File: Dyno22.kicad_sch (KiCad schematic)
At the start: 50 parts, among them J1 Pwr Input, J2 Display, J3 Pwr Output, J4 BPM & Sensors, J7 UART, SW1 SW_DPST_x2, U1 TS2937CW50, U2 LM324, U3 Demux

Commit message: Amplifier footprint changes
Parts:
- U2: footprint SOIC:SOIC-14_W3.9mm -> Package_DIP:DIP-14_W7.62mm
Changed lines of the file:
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@@
       (effects (font (size 1.27 1.27)) (justify left))
     )
-    (property "Footprint" "SOIC:SOIC-14_W3.9mm" (at 240.03 149.86 0)
+    (property "Footprint" "Package_DIP:DIP-14_W7.62mm" (at 240.03 149.86 0)
       (effects (font (size 1.27 1.27)) hide)
     )
-    (property "Datasheet" "http://www.ti.com/lit/ds/symlink/lm321.pdf" (at 241.3 152.4 0)
+    (property "Datasheet" "https://www.ti.com/lit/ds/symlink/lm224.pdf?HQS=dis-dk-null-digikeymode-dsf-pf-null-wwe&ts=1705778607350" (at 241.3 152.4 0)
       (effects (font (size 1.27 1.27)) hide)
     )

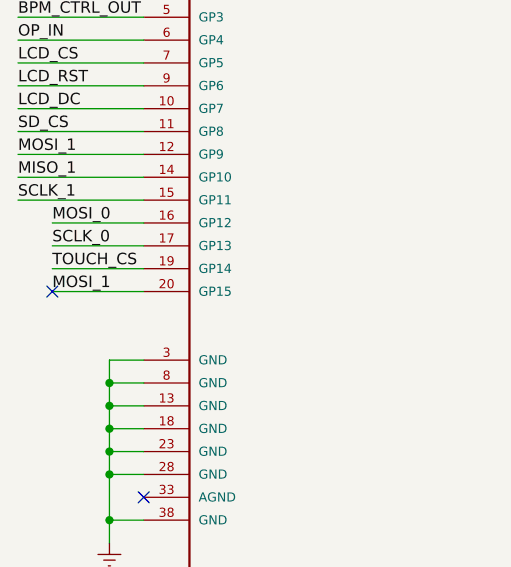
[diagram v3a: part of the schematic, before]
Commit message: Forgot to save schematic changes
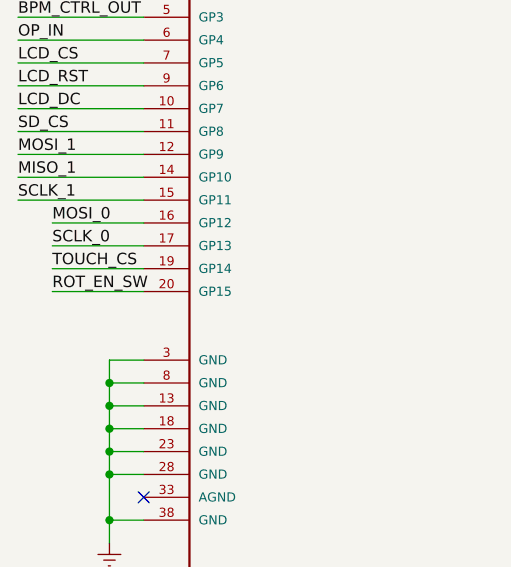
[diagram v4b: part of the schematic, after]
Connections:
- net MOSI_1: no longer A1.20 (GP15)
- net ROT_EN_SW: now also A1.20 (GP15)
- no-connect marks 16 -> 15
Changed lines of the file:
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@@
   (no_connect (at 127 50.8))
   (no_connect (at 63.5 132.08))
-  (no_connect (at 20.32 83.82))
   (no_connect (at 86.36 99.06))
   (no_connect (at 154.94 193.04))
@@
     (effects (font (size 1.27 1.27)) (justify left bottom))
   )
-  (label "MOSI_1" (at 20.32 83.82 0) (fields_autoplaced)
+  (label "ROT_EN_SW" (at 20.32 83.82 0) (fields_autoplaced)
     (effects (font (size 1.27 1.27)) (justify left bottom))
   )
@@
       (effects (font (size 1.27 1.27) italic) hide)
     )
-    (property "Datasheet" "http://www.ti.com/lit/ds/symlink/lm2937.pdf" (at 160.02 40.64 0)
-      (effects (font (size 1.27 1.27)) hide)
-    )
+    (property "Datasheet" "https://services.ts.com.tw/storage/resources/datasheet/TS2937_E15.pdf" (at 160.02 40.64 0)
+      (effects (font (size 1.27 1.27)) hide)
+    )

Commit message: Fix the earth, the earth is our home
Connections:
- net +24V: no longer TP1.1
- net 20V_IN: now reaches F1.1, J1.2 (Pin_2)
- net 20V_IN: now also TP1.1
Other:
- moved on the sheet: TP1

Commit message: Through hole adjustments and some routing changes
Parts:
- TP2, TP3: footprint TestPoint:TestPoint_Loop_D2.60mm_Drill1.6mm_Beaded -> TestPoint:TestPoint_Plated_Hole_D2.0mm
- TP4, TP5: footprint TestPoint:TestPoint_Loop_D2.60mm_Drill1.4mm_Beaded -> TestPoint:TestPoint_Plated_Hole_D2.0mm
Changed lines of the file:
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@@
       (effects (font (size 1.27 1.27)) (justify left))
     )
-    (property "Footprint" "TestPoint:TestPoint_Loop_D2.60mm_Drill1.6mm_Beaded" (at 176.53 22.86 0)
+    (property "Footprint" "TestPoint:TestPoint_Plated_Hole_D2.0mm" (at 176.53 22.86 0)
       (effects (font (size 1.27 1.27)) hide)
     )
@@
       (effects (font (size 1.27 1.27)) (justify left))
     )
-    (property "Footprint" "TestPoint:TestPoint_Loop_D2.60mm_Drill1.4mm_Beaded" (at 130.81 172.72 0)
+    (property "Footprint" "TestPoint:TestPoint_Plated_Hole_D2.0mm" (at 130.81 172.72 0)
       (effects (font (size 1.27 1.27)) hide)
     )
@@
       (effects (font (size 1.27 1.27)) (justify left))
     )
-    (property "Footprint" "TestPoint:TestPoint_Loop_D2.60mm_Drill1.6mm_Beaded" (at 92.71 48.26 0)
+    (property "Footprint" "TestPoint:TestPoint_Plated_Hole_D2.0mm" (at 92.71 48.26 0)
       (effects (font (size 1.27 1.27)) hide)
     )
@@
       (effects (font (size 1.27 1.27)) (justify left))
     )
-    (property "Footprint" "TestPoint:TestPoint_Loop_D2.60mm_Drill1.4mm_Beaded" (at 138.43 63.5 0)
-      (effects (font (size 1.27 1.27)) hide)
-    )
+    (property "Footprint" "TestPoint:TestPoint_Plated_Hole_D2.0mm" (at 138.43 63.5 0)
+      (effects (font (size 1.27 1.27)) hide)
+    )

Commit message: updated encoder
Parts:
- C2: footprint Capacitor_Tantalum_SMD:CP_EIA-6032-20_AVX-F -> CAP_293D-C_VSS:CAP_293D-C_VSS
- Encoder1: footprint Rotary_Encoder:RotaryEncoder_Alps_EC12E-Switch_Vertical_H20mm_CircularMountingHoles -> PEC11R_4215F_S0024:TO_215F-S0024; symbol Device:RotaryEncoder_Switch -> Rotary_Encoder_Kevin:PEC11R-4215F-S0024
- TP1: footprint TestPoint:TestPoint_Loop_D2.60mm_Drill1.4mm_Beaded -> TestPoint:TestPoint_Plated_Hole_D2.0mm
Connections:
- net Earth: now also Encoder1.1, Encoder1.B; no longer Encoder1.C, Encoder1.S2
- net ROT_EN_B: now also Encoder1.C; no longer Encoder1.B
- net ROT_EN_SW: now also Encoder1.2; no longer Encoder1.S1
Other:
- moved on the sheet: TP5
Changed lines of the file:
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@@
   (junction (at 228.6 133.35) (diameter 0) (color 0 0 0 0)
   )
-  (junction (at 130.81 167.64) (diameter 0) (color 0 0 0 0)
-  )
   (junction (at 26.67 93.98) (diameter 0) (color 0 0 0 0)
   )
@@
   (junction (at 127 104.14) (diameter 0) (color 0 0 0 0)
   )
-  (junction (at 130.81 144.78) (diameter 0) (color 0 0 0 0)
-  )
   (junction (at 225.425 108.585) (diameter 0) (color 0 0 0 0)
   )
   (junction (at 85.09 114.3) (diameter 0) (color 0 0 0 0)
   )
+  (junction (at 156.21 143.51) (diameter 0) (color 0 0 0 0)
+  )
   (junction (at 26.67 101.6) (diameter 0) (color 0 0 0 0)
   )
@@
   (junction (at 220.98 52.07) (diameter 0) (color 0 0 0 0)
   )
+  (junction (at 156.21 167.64) (diameter 0) (color 0 0 0 0)
+  )
   (junction (at 26.67 109.22) (diameter 0) (color 0 0 0 0)
   )
@@
     (stroke (width 0) (type default))
   )
+  (wire (pts (xy 156.21 143.51) (xy 156.21 153.67))
+    (stroke (width 0) (type default))
+  )
   (wire (pts (xy 264.16 67.31) (xy 273.685 67.31))
     (stroke (width 0) (type default))
@@
     (stroke (width 0) (type default))
   )
+  (wire (pts (xy 156.21 167.64) (xy 156.21 156.21))
+    (stroke (width 0) (type default))
+  )
   (wire (pts (xy 20.32 78.74) (xy 30.48 78.74))
     (stroke (width 0) (type default))
@@
     (stroke (width 0) (type default))
   )
-  (wire (pts (xy 130.81 151.13) (xy 130.81 144.78))
-    (stroke (width 0) (type default))
-  )
   (wire (pts (xy 260.985 116.205) (xy 272.415 116.205))
     (stroke (width 0) (type default))
@@
     (stroke (width 0) (type default))
   )
-  (wire (pts (xy 114.3 167.64) (xy 130.81 167.64))
+  (wire (pts (xy 114.3 167.64) (xy 156.21 167.64))
     (stroke (width 0) (type default))
   )
@@
     (stroke (width 0) (type default))
   )
-  (wire (pts (xy 120.65 144.78) (xy 130.81 144.78))
-    (stroke (width 0) (type default))
-  )
   (wire (pts (xy 264.16 72.39) (xy 273.685 72.39))
     (stroke (width 0) (type default))
@@
     (stroke (width 0) (type default))
   )
+  (wire (pts (xy 156.21 143.51) (xy 160.02 143.51))
+    (stroke (width 0) (type default))
+  )
   (wire (pts (xy 133.35 63.5) (xy 133.35 64.77))
     (stroke (width 0) (type default))
@@
     (stroke (width 0) (type default))
   )
-  (wire (pts (xy 130.81 167.64) (xy 130.81 156.21))
-    (stroke (width 0) (type default))
-  )
   (wire (pts (xy 85.09 114.3) (xy 85.09 116.84))
     (stroke (width 0) (type default))
@@
     (stroke (width 0) (type default))
   )
-  (wire (pts (xy 137.16 144.78) (xy 130.81 144.78))
+  (wire (pts (xy 120.65 143.51) (xy 156.21 143.51))
     (stroke (width 0) (type default))
   )
@@
     (stroke (width 0) (type default))
   )
-  (wire (pts (xy 120.65 143.51) (xy 120.65 144.78))
-    (stroke (width 0) (type default))
-  )
   (wire (pts (xy 181.61 152.4) (xy 190.5 152.4))
     (stroke (width 0) (type default))
@@
     (effects (font (size 1.27 1.27)) (justify left bottom))
   )
-  (label "ROT_EN_SW" (at 137.16 144.78 0) (fields_autoplaced)
+  (label "ROT_EN_SW" (at 160.02 143.51 0) (fields_autoplaced)
     (effects (font (size 1.27 1.27)) (justify left bottom))
   )
@@
       (effects (font (size 1.27 1.27)) (justify left))
     )
-    (property "Footprint" "Capacitor_Tantalum_SMD:CP_EIA-6032-20_AVX-F" (at 143.51 43.18 0)
+    (property "Footprint" "CAP_293D-C_VSS:CAP_293D-C_VSS" (at 143.51 43.18 0)
       (effects (font (size 1.27 1.27)) hide)
     )
-    (property "Datasheet" "~" (at 143.51 43.18 0)
+    (property "Datasheet" "https://www.vishay.com/docs/40002/293d.pdf" (at 143.51 43.18 0)
       (effects (font (size 1.27 1.27)) hide)
     )
@@
     )
   )
-  (symbol (lib_id "Connector:TestPoint") (at 130.81 167.64 270) (unit 1)
+  (symbol (lib_id "Connector:TestPoint") (at 156.21 167.64 270) (unit 1)
     (in_bom yes) (on_board yes) (dnp no) (fields_autoplaced)
-    (property "Reference" "TP5" (at 135.89 166.37 90)
+    (property "Reference" "TP5" (at 161.29 166.37 90)
       (effects (font (size 1.27 1.27)) (justify left))
     )
-    (property "Value" "GND_TestPoint" (at 135.89 168.91 90)
+    (property "Value" "GND_TestPoint" (at 161.29 168.91 90)
       (effects (font (size 1.27 1.27)) (justify left))
     )
-    (property "Footprint" "TestPoint:TestPoint_Plated_Hole_D2.0mm" (at 130.81 172.72 0)
+    (property "Footprint" "TestPoint:TestPoint_Plated_Hole_D2.0mm" (at 156.21 172.72 0)
       (effects (font (size 1.27 1.27)) hide)
     )
-    (property "Datasheet" "~" (at 130.81 172.72 0)
+    (property "Datasheet" "~" (at 156.21 172.72 0)
       (effects (font (size 1.27 1.27)) hide)
     )
@@
       (effects (font (size 1.27 1.27)))
     )
-    (property "Footprint" "TestPoint:TestPoint_Loop_D2.60mm_Drill1.4mm_Beaded" (at 109.22 45.72 0)
+    (property "Footprint" "TestPoint:TestPoint_Plated_Hole_D2.0mm" (at 109.22 45.72 0)
       (effects (font (size 1.27 1.27)) hide)
     )
@@
     )
   )
-  (symbol (lib_id "Device:RotaryEncoder_Switch") (at 123.19 153.67 0) (unit 1)
+  (symbol (lib_id "Rotary_Encoder_Kevin:PEC11R-4215F-S0024") (at 156.21 156.21 180) (unit 1)
     (in_bom yes) (on_board yes) (dnp no)
-    (property "Reference" "Encoder1" (at 107.95 173.99 0)
+    (property "Reference" "Encoder1" (at 138.43 142.24 0)
       (effects (font (size 1.27 1.27)))
     )
-    (property "Value" "RotaryEncoder_Switch" (at 107.95 176.53 0)
+    (property "Value" "RotaryEncoder_Switch" (at 139.7 139.7 0)
       (effects (font (size 1.27 1.27)))
     )
-    (property "Footprint" "Rotary_Encoder:RotaryEncoder_Alps_EC12E-Switch_Vertical_H20mm_CircularMountingHoles" (at 119.38 149.606 0)
-      (effects (font (size 1.27 1.27)) hide)
+    (property "Footprint" "PEC11R_4215F_S0024:TO_215F-S0024" (at 156.21 156.21 0)
+      (effects (font (size 1.27 1.27) italic) hide)
     )
-    (property "Datasheet" "~" (at 123.19 147.066 0)
-      (effects (font (size 1.27 1.27)) hide)
+    (property "Datasheet" "PEC11R-4215F-S0024" (at 156.21 156.21 0)
+      (effects (font (size 1.27 1.27) italic) hide)
     )
+    (pin "1")
+    (pin "2")
     (pin "A")
     (pin "B")
     (pin "C")
-    (pin "S1")
-    (pin "S2")
     (instances
       (project "Dyno22"

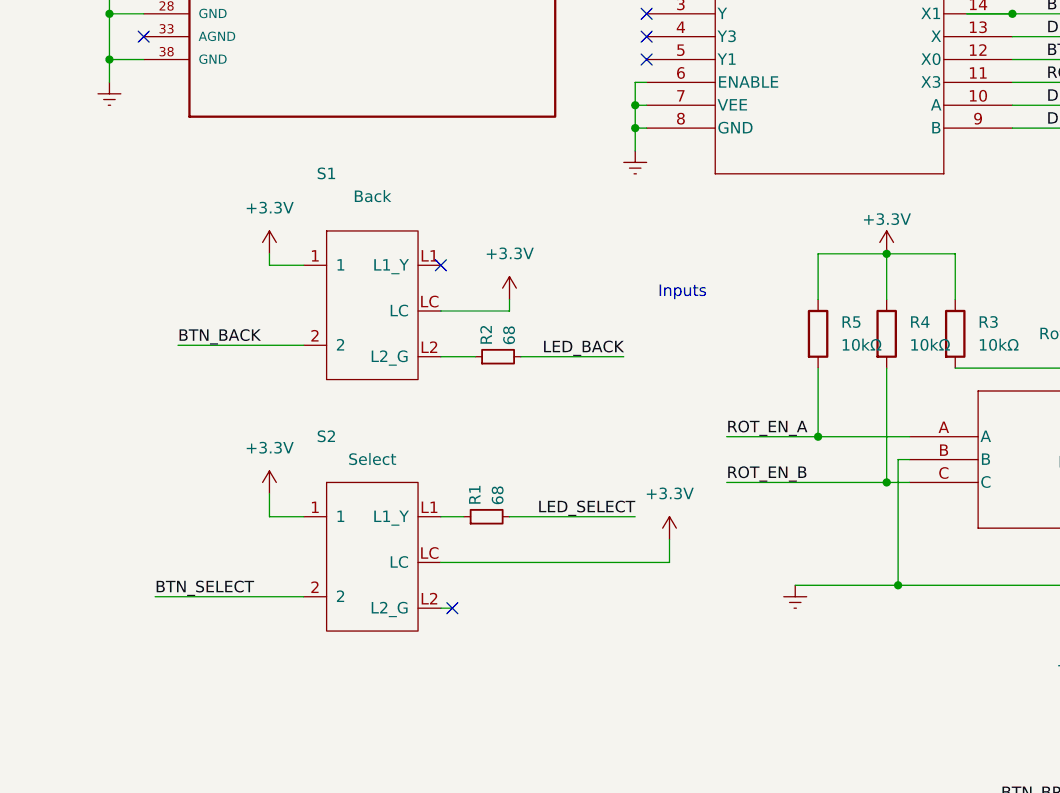
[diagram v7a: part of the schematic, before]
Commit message: added encoder filter circuit
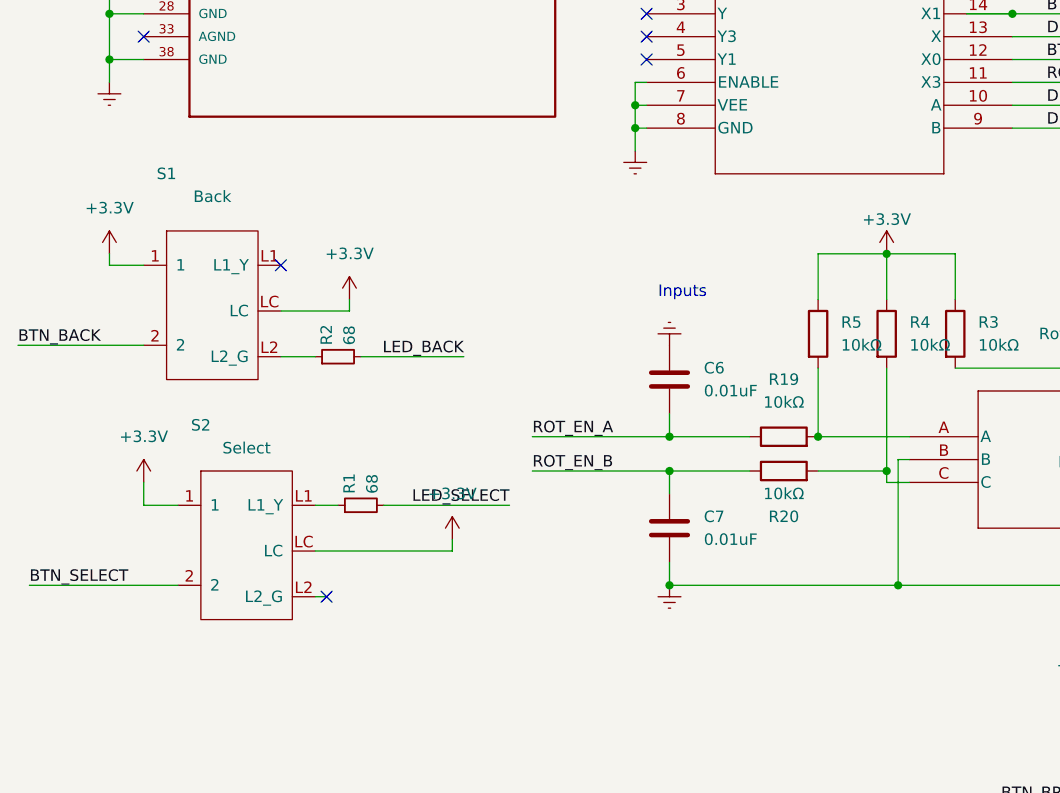
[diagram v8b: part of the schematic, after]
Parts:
- added C6, C7: 0.01uF, Capacitor_SMD:C_0603_1608Metric, symbol Device:C
- added R19, R20: 10kΩ, Resistor_SMD:R_0805_2012Metric, symbol Device:R
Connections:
- net Earth: now also C6.1, C7.2
- net ROT_EN_A: now also C6.2, R19.1; no longer Encoder1.A, R5.2
- net ROT_EN_B: now also C7.1, R20.1; no longer Encoder1.C, R4.2
- new net: Encoder1.A, R19.2, R5.2
- new net: Encoder1.C, R20.2, R4.2
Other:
- moved on the sheet: R1, R2, S1, S2
